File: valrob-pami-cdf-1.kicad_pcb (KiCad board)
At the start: 4 copper layers, 58 x 50 mm, 139 parts, among them J1 Conn_01x04, J2 USB_C_Receptacle_USB2.0_14P, J3 Conn_01x02, J4 Conn_01x04_Pin, J5 Conn_01x06, M1 Motor_Servo, M2 Stepper_Motor_bipolar, M3 Stepper_Motor_bipolar, Q1 Q_NMOS, Q2 Q_NMOS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

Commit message: schem/pcb: reorganize programmable gpios
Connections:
- U4 pad 10: /SDA -> /~{FAULT_1}
- U4 pad 11: /SCL -> unconnected-(U4-GPIO6/ADC1_CH5-Pad11)
- U4 pad 12: /DIR_1 -> /EMS
- U4 pad 13: /STEP_1 -> /VPWM_1
- U4 pad 14: /EN_1 -> /VPWM_2
- U4 pad 15: /~{SLEEP_1} -> /Vsense
- U4 pad 16: /~{FAULT_1} -> /DIR_2
- U4 pad 17: /DIR_2 -> /STEP_2
- U4 pad 18: /STEP_2 -> /EN_2
- U4 pad 19: /EN_2 -> /~{SLEEP_2}
- U4 pad 23: /~{SLEEP_2} -> /~{FAULT_2}
- U4 pad 24: /~{FAULT_2} -> /BUZZER
- U4 pad 27: /BUZZER -> /RGB1
- U4 pad 36: /RGB1 -> /SCL
- U4 pad 37: /SERVO1 -> /SDA
- U4 pad 43: unconnected-(U4-GPIO38-Pad43) -> /SERVO1
- U4 pad 6: /EMS -> /DIR_1
- U4 pad 7: /Vsense -> /STEP_1
- U4 pad 8: /VPWM_1 -> /EN_1
- U4 pad 9: /VPWM_2 -> /~{SLEEP_1}
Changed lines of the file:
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@@
 	(net 109 "unconnected-(U4-MTDO{slash}JTAG{slash}GPIO40-Pad45)")
 	(net 110 "unconnected-(U4-GPIO45-Pad51)")
-	(net 111 "unconnected-(U4-GPIO38-Pad43)")
-	(net 112 "unconnected-(U4-SPIQ{slash}GPIO31-Pad34)")
-	(net 113 "/~{SLEEP_2}")
-	(net 114 "unconnected-(U4-GPIO16{slash}ADC2_CH5{slash}XTAL_32K_N-Pad22)")
-	(net 115 "unconnected-(U4-MTDI{slash}JTAG{slash}GPIO41-Pad47)")
-	(net 116 "unconnected-(U6-M1-Pad17)")
-	(net 117 "unconnected-(U6-TOFF-Pad14)")
-	(net 118 "unconnected-(U7-TOFF-Pad14)")
-	(net 119 "unconnected-(U7-M1-Pad17)")
-	(net 120 "unconnected-(D1-DOUT-Pad2)")
-	(net 121 "Net-(J5-Pin_5)")
-	(net 122 "Net-(J5-Pin_4)")
-	(net 123 "Net-(J5-Pin_2)")
-	(net 124 "Net-(J5-Pin_3)")
+	(net 111 "unconnected-(U4-SPIQ{slash}GPIO31-Pad34)")
+	(net 112 "/~{SLEEP_2}")
+	(net 113 "unconnected-(U4-GPIO16{slash}ADC2_CH5{slash}XTAL_32K_N-Pad22)")
+	(net 114 "unconnected-(U4-MTDI{slash}JTAG{slash}GPIO41-Pad47)")
+	(net 115 "unconnected-(U6-M1-Pad17)")
+	(net 116 "unconnected-(U6-TOFF-Pad14)")
+	(net 117 "unconnected-(U7-TOFF-Pad14)")
+	(net 118 "unconnected-(U7-M1-Pad17)")
+	(net 119 "unconnected-(D1-DOUT-Pad2)")
+	(net 120 "Net-(J5-Pin_5)")
+	(net 121 "Net-(J5-Pin_4)")
+	(net 122 "Net-(J5-Pin_2)")
+	(net 123 "Net-(J5-Pin_3)")
+	(net 124 "unconnected-(U4-GPIO6{slash}ADC1_CH5-Pad11)")
 	(footprint "GLCS:Texas_RGE0024B_VQFN-24-1EP_4x4mm_P0.5mm_EP2.5x2.5mm_ThermalVias"
 		(layer "F.Cu")
@@
 			(layers "F.Cu" "F.Mask" "F.Paste")
 			(roundrect_rratio 0.25)
-			(net 117 "unconnected-(U6-TOFF-Pad14)")
+			(net 116 "unconnected-(U6-TOFF-Pad14)")
 			(pinfunction "TOFF")
 			(pintype "input+no_connect")
@@
 			(layers "F.Cu" "F.Mask" "F.Paste")
 			(roundrect_rratio 0.25)
-			(net 116 "unconnected-(U6-M1-Pad17)")
+			(net 115 "unconnected-(U6-M1-Pad17)")
 			(pinfunction "M1")
 			(pintype "input+no_connect")
@@
 			(layers "F.Cu" "F.Mask" "F.Paste")
 			(roundrect_rratio 0.1)
-			(net 120 "unconnected-(D1-DOUT-Pad2)")
+			(net 119 "unconnected-(D1-DOUT-Pad2)")
 			(pinfunction "DOUT")
 			(pintype "output+no_connect")
@@
 			(layers "F.Cu" "F.Mask" "F.Paste")
 			(roundrect_rratio 0.25)
-			(net 118 "unconnected-(U7-TOFF-Pad14)")
+			(net 117 "unconnected-(U7-TOFF-Pad14)")
 			(pinfunction "TOFF")
 			(pintype "input+no_connect")
@@
 			(layers "F.Cu" "F.Mask" "F.Paste")
 			(roundrect_rratio 0.25)
-			(net 119 "unconnected-(U7-M1-Pad17)")
+			(net 118 "unconnected-(U7-M1-Pad17)")
 			(pinfunction "M1")
 			(pintype "input+no_connect")
@@
 			(layers "F.Cu" "F.Mask" "F.Paste")
 			(roundrect_rratio 0.25)
-			(net 113 "/~{SLEEP_2}")
+			(net 112 "/~{SLEEP_2}")
 			(pinfunction "~{SLEEP}")
 			(pintype "input")
@@
 			(layers "F.Cu" "F.Mask" "F.Paste")
 			(roundrect_rratio 0.25)
-			(net 87 "/EMS")
+			(net 93 "/DIR_1")
 			(pinfunction "GPIO1/ADC1_CH0")
 			(pintype "bidirectional")
@@
 			(layers "F.Cu" "F.Mask" "F.Paste")
 			(roundrect_rratio 0.25)
-			(net 23 "/Vsense")
+			(net 88 "/STEP_1")
 			(pinfunction "GPIO2/ADC1_CH1")
 			(pintype "bidirectional")
@@
 			(layers "F.Cu" "F.Mask" "F.Paste")
 			(roundrect_rratio 0.25)
-			(net 84 "/VPWM_1")
+			(net 100 "/EN_1")
 			(pinfunction "GPIO3/ADC1_CH2")
 			(pintype "bidirectional")
@@
 			(layers "F.Cu" "F.Mask" "F.Paste")
 			(roundrect_rratio 0.25)
-			(net 86 "/VPWM_2")
+			(net 99 "/~{SLEEP_1}")
 			(pinfunction "GPIO4/ADC1_CH3")
 			(pintype "bidirectional")
@@
 			(layers "F.Cu" "F.Mask" "F.Paste")
 			(roundrect_rratio 0.25)
-			(net 81 "/SDA")
+			(net 83 "/~{FAULT_1}")
 			(pinfunction "GPIO5/ADC1_CH4")
 			(pintype "bidirectional")
@@
 			(layers "F.Cu" "F.Mask" "F.Paste")
 			(roundrect_rratio 0.25)
-			(net 82 "/SCL")
+			(net 124 "unconnected-(U4-GPIO6{slash}ADC1_CH5-Pad11)")
 			(pinfunction "GPIO6/ADC1_CH5")
 			(pintype "bidirectional")
@@
 			(layers "F.Cu" "F.Mask" "F.Paste")
 			(roundrect_rratio 0.25)
-			(net 93 "/DIR_1")
+			(net 87 "/EMS")
 			(pinfunction "GPIO7/ADC1_CH6")
 			(pintype "bidirectional")
@@
 			(layers "F.Cu" "F.Mask" "F.Paste")
 			(roundrect_rratio 0.25)
-			(net 88 "/STEP_1")
+			(net 84 "/VPWM_1")
 			(pinfunction "GPIO8/ADC1_CH7")
 			(pintype "bidirectional")
@@
 			(layers "F.Cu" "F.Mask" "F.Paste")
 			(roundrect_rratio 0.25)
-			(net 100 "/EN_1")
+			(net 86 "/VPWM_2")
 			(pinfunction "GPIO9/ADC1_CH8")
 			(pintype "bidirectional")
@@
 			(layers "F.Cu" "F.Mask" "F.Paste")
 			(roundrect_rratio 0.25)
-			(net 99 "/~{SLEEP_1}")
+			(net 23 "/Vsense")
 			(pinfunction "GPIO10/ADC1_CH9")
 			(pintype "bidirectional")
@@
 			(layers "F.Cu" "F.Mask" "F.Paste")
 			(roundrect_rratio 0.25)
-			(net 83 "/~{FAULT_1}")
+			(net 104 "/DIR_2")
 			(pinfunction "GPIO11/ADC2_CH0")
 			(pintype "bidirectional")
@@
 			(layers "F.Cu" "F.Mask" "F.Paste")
 			(roundrect_rratio 0.25)
-			(net 104 "/DIR_2")
+			(net 97 "/STEP_2")
 			(pinfunction "GPIO12/ADC2_CH1")
 			(pintype "bidirectional")
@@
 			(layers "F.Cu" "F.Mask" "F.Paste")
 			(roundrect_rratio 0.25)
-			(net 97 "/STEP_2")
+			(net 106 "/EN_2")
 			(pinfunction "GPIO13/ADC2_CH2")
 			(pintype "bidirectional")
@@
 			(layers "F.Cu" "F.Mask" "F.Paste")
 			(roundrect_rratio 0.25)
-			(net 106 "/EN_2")
+			(net 112 "/~{SLEEP_2}")
 			(pinfunction "GPIO14/ADC2_CH3")
 			(pintype "bidirectional")
@@
 			(layers "F.Cu" "F.Mask" "F.Paste")
 			(roundrect_rratio 0.25)
-			(net 114 "unconnected-(U4-GPIO16{slash}ADC2_CH5{slash}XTAL_32K_N-Pad22)")
+			(net 113 "unconnected-(U4-GPIO16{slash}ADC2_CH5{slash}XTAL_32K_N-Pad22)")
 			(pinfunction "GPIO16/ADC2_CH5/XTAL_32K_N")
 			(pintype "bidirectional+no_connect")
@@
 			(layers "F.Cu" "F.Mask" "F.Paste")
 			(roundrect_rratio 0.25)
-			(net 113 "/~{SLEEP_2}")
+			(net 85 "/~{FAULT_2}")
 			(pinfunction "GPIO17/ADC2_CH6")
 			(pintype "bidirectional")
@@
 			(layers "F.Cu" "F.Mask" "F.Paste")
 			(roundrect_rratio 0.25)
-			(net 85 "/~{FAULT_2}")
+			(net 75 "/BUZZER")
 			(pinfunction "GPIO18/ADC2_CH7")
 			(pintype "bidirectional")
@@
 			(layers "F.Cu" "F.Mask" "F.Paste")
 			(roundrect_rratio 0.25)
-			(net 75 "/BUZZER")
+			(net 37 "/RGB1")
 			(pinfunction "GPIO21")
 			(pintype "bidirectional")
@@
 			(layers "F.Cu" "F.Mask" "F.Paste")
 			(roundrect_rratio 0.25)
-			(net 112 "unconnected-(U4-SPIQ{slash}GPIO31-Pad34)")
+			(net 111 "unconnected-(U4-SPIQ{slash}GPIO31-Pad34)")
 			(pinfunction "SPIQ/GPIO31")
 			(pintype "bidirectional+no_connect")
@@
 			(layers "F.Cu" "F.Mask" "F.Paste")
 			(roundrect_rratio 0.25)
-			(net 37 "/RGB1")
+			(net 82 "/SCL")
 			(pinfunction "SPICLK_N/GPIO48")
 			(pintype "bidirectional")
@@
 			(layers "F.Cu" "F.Mask" "F.Paste")
 			(roundrect_rratio 0.25)
-			(net 54 "/SERVO1")
+			(net 81 "/SDA")
 			(pinfunction "SPICLK_P/GPIO47")
 			(pintype "bidirectional")
@@
 			(layers "F.Cu" "F.Mask" "F.Paste")
 			(roundrect_rratio 0.25)
-			(net 123 "Net-(J5-Pin_2)")
+			(net 122 "Net-(J5-Pin_2)")
 			(pinfunction "GPIO34")
 			(pintype "bidirectional")
@@
 			(layers "F.Cu" "F.Mask" "F.Paste")
 			(roundrect_rratio 0.25)
-			(net 124 "Net-(J5-Pin_3)")
+			(net 123 "Net-(J5-Pin_3)")
 			(pinfunction "GPIO35")
 			(pintype "bidirectional")
@@
 			(layers "F.Cu" "F.Mask" "F.Paste")
 			(roundrect_rratio 0.25)
-			(net 122 "Net-(J5-Pin_4)")
+			(net 121 "Net-(J5-Pin_4)")
 			(pinfunction "GPIO36")
 			(pintype "bidirectional")
@@
 			(layers "F.Cu" "F.Mask" "F.Paste")
 			(roundrect_rratio 0.25)
-			(net 121 "Net-(J5-Pin_5)")
+			(net 120 "Net-(J5-Pin_5)")
 			(pinfunction "GPIO37")
 			(pintype "bidirectional")
@@
 			(layers "F.Cu" "F.Mask" "F.Paste")
 			(roundrect_rratio 0.25)
-			(net 111 "unconnected-(U4-GPIO38-Pad43)")
+			(net 54 "/SERVO1")
 			(pinfunction "GPIO38")
-			(pintype "bidirectional+no_connect")
+			(pintype "bidirectional")
 		)
 		(pad "44" smd roundrect
@@
 			(layers "F.Cu" "F.Mask" "F.Paste")
 			(roundrect_rratio 0.25)
-			(net 115 "unconnected-(U4-MTDI{slash}JTAG{slash}GPIO41-Pad47)")
+			(net 114 "unconnected-(U4-MTDI{slash}JTAG{slash}GPIO41-Pad47)")
 			(pinfunction "MTDI/JTAG/GPIO41")
 			(pintype "bidirectional+no_connect")
@@
 			(layers "*.Cu" "*.Mask")
 			(remove_unused_layers no)
-			(net 123 "Net-(J5-Pin_2)")
+			(net 122 "Net-(J5-Pin_2)")
 			(pinfunction "Pin_2")
 			(pintype "passive")
@@
 			(layers "*.Cu" "*.Mask")
 			(remove_unused_layers no)
-			(net 124 "Net-(J5-Pin_3)")
+			(net 123 "Net-(J5-Pin_3)")
 			(pinfunction "Pin_3")
 			(pintype "passive")
@@
 			(layers "*.Cu" "*.Mask")
 			(remove_unused_layers no)
-			(net 122 "Net-(J5-Pin_4)")
+			(net 121 "Net-(J5-Pin_4)")
 			(pinfunction "Pin_4")
 			(pintype "passive")
@@
 			(layers "*.Cu" "*.Mask")
 			(remove_unused_layers no)
-			(net 121 "Net-(J5-Pin_5)")
+			(net 120 "Net-(J5-Pin_5)")
 			(pinfunction "Pin_5")
 			(pintype "passive")

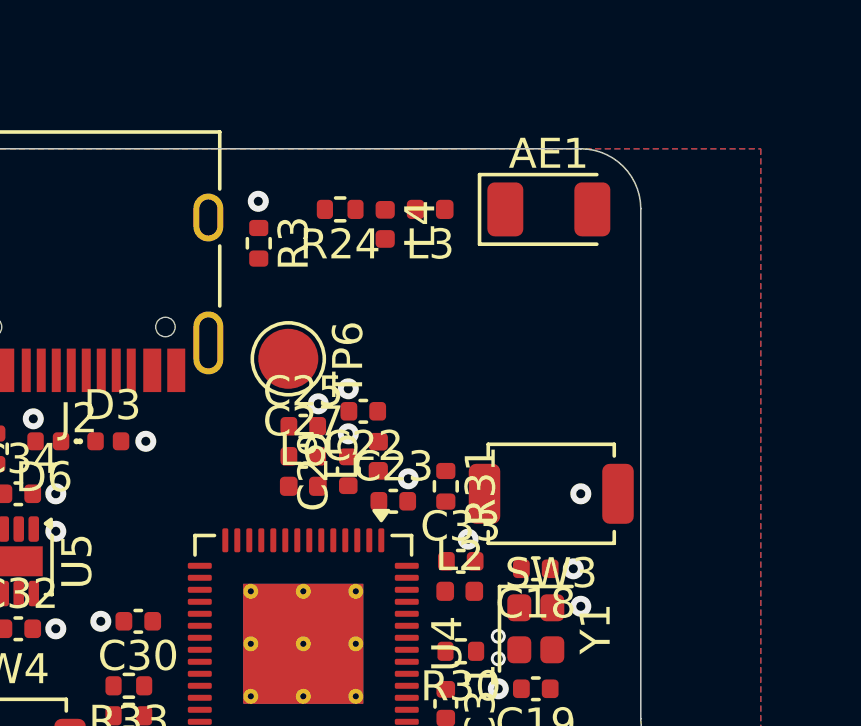
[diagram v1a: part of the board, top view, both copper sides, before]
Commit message: pcb: add rf routing
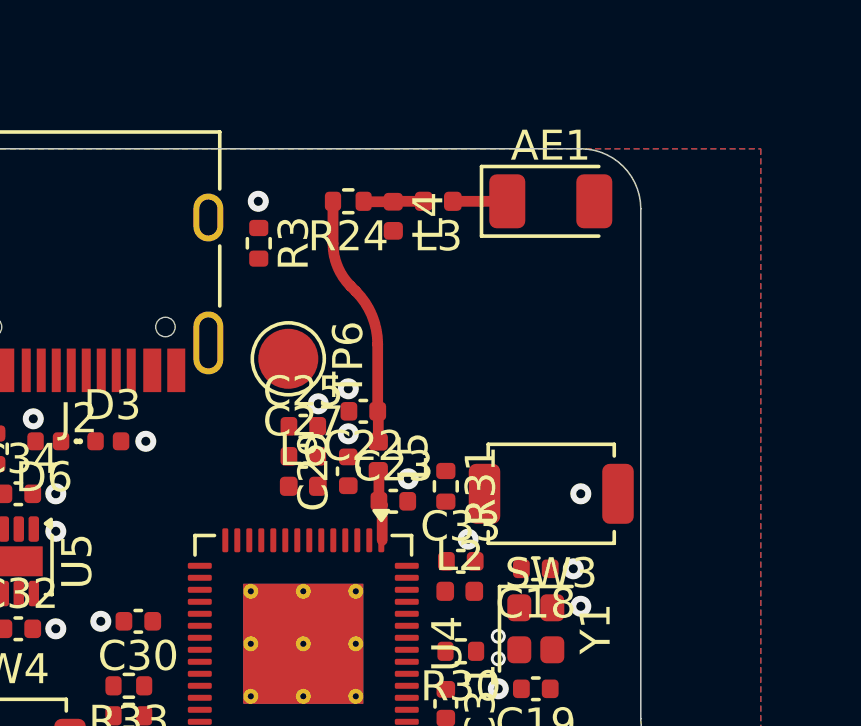
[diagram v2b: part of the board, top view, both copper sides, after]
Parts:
- moved L3 0.38 mm to (173.2, 74.8)
- moved L4 0.38 mm to (171.8, 75.2)
- moved R24 0.38 mm to (170.2, 74.8)
- moved AE1 0.28 mm to (177.0, 74.8)
- turned L5 to -90 degrees
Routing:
- net /RF_TRANS: track 0.00 -> 8.42 mm
- net /RF_ESP: track 0.00 -> 2.37 mm
- net Net-(L3-Pad2): track 0.00 -> 2.02 mm
- net /RF_ANT: track 0.00 -> 1.81 mm
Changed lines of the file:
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@@
 	(footprint "Inductor_SMD:L_0402_1005Metric"
 		(layer "F.Cu")
-		(at 171.25 83.25 90)
+		(at 171.25 83.25 -90)
 		(descr "Inductor SMD 0402 (1005 Metric), square (rectangular) end terminal, IPC-7351 nominal, (Body size source: http://www.tortai-tech.com/upload/download/2011102023233369053.pdf), generated with kicad-footprint-generator")
 		(tags "inductor")
@@
 		)
 		(property "Manufacturer" "Murata"
-			(at 0 0 90)
+			(at 0 0 270)
 			(unlocked yes)
 			(layer "F.Fab")
@@
 		)
 		(property "Manufacturer Part Number" "LQG15HS2N7S02D"
-			(at 0 0 90)
+			(at 0 0 270)
 			(unlocked yes)
 			(layer "F.Fab")
@@
 		)
 		(property "Basic" "X"
-			(at 0 0 90)
+			(at 0 0 270)
 			(unlocked yes)
 			(layer "F.Fab")
@@
 		)
 		(property "JLCPCB Part #" "C77108"
-			(at 0 0 90)
+			(at 0 0 270)
 			(unlocked yes)
 			(layer "F.Fab")
@@
 		)
 		(pad "1" smd roundrect
-			(at -0.485 0 90)
+			(at -0.485 0 270)
 			(size 0.59 0.64)
 			(layers "F.Cu" "F.Mask" "F.Paste")
@@
 		)
 		(pad "2" smd roundrect
-			(at 0.485 0 90)
+			(at 0.485 0 270)
 			(size 0.59 0.64)
 			(layers "F.Cu" "F.Mask" "F.Paste")
@@
 	(footprint "Inductor_SMD:L_0402_1005Metric"
 		(layer "F.Cu")
-		(at 172.98 75.02 180)
+		(at 173.25 74.75 180)
 		(descr "Inductor SMD 0402 (1005 Metric), square (rectangular) end terminal, IPC-7351 nominal, (Body size source: http://www.tortai-tech.com/upload/download/2011102023233369053.pdf), generated with kicad-footprint-generator")
 		(tags "inductor")
@@
 	(footprint "RF_Antenna:Johanson_2450AT18x100"
 		(layer "F.Cu")
-		(at 176.935 75.02)
+		(at 177 74.75)
 		(descr "Johanson 2450AT43F0100 SMD antenna 2400-2500Mhz, -0.5dBi, https://www.johansontechnology.com/datasheets/2450AT18A100/2450AT18A100.pdf")
 		(tags "antenna")
@@
 	(footprint "Inductor_SMD:L_0402_1005Metric"
 		(layer "F.Cu")
-		(at 171.48 75.52 -90)
+		(at 171.75 75.25 -90)
 		(descr "Inductor SMD 0402 (1005 Metric), square (rectangular) end terminal, IPC-7351 nominal, (Body size source: http://www.tortai-tech.com/upload/download/2011102023233369053.pdf), generated with kicad-footprint-generator")
 		(tags "inductor")
@@
 	(footprint "Resistor_SMD:R_0402_1005Metric"
 		(layer "F.Cu")
-		(at 169.98 75.02 180)
+		(at 170.25 74.75 180)
 		(descr "Resistor SMD 0402 (1005 Metric), square (rectangular) end terminal, IPC-7351 nominal, (Body size source: IPC-SM-782 page 72, https://www.pcb-3d.com/wordpress/wp-content/uploads/ipc-sm-782a_amendment_1_and_2.pdf), generated with kicad-footprint-generator")
 		(tags "resistor")
@@
 		(layer "Edge.Cuts")
 	)
+	(segment
+		(start 175.55 74.75)
+		(end 173.735 74.75)
+		(width 0.359)
+		(layer "F.Cu")
+		(net 1)
+	)
 	(via
 		(at 161 105.75)
@@
 		(net 4)
 	)
+	(segment
+		(start 169.74 74.75)
+		(end 169.74 76.161573)
+		(width 0.359)
+		(layer "F.Cu")
+		(net 20)
+	)
+	(segment
+		(start 171.25 82.765)
+		(end 171.25 81.77)
+		(width 0.359)
+		(layer "F.Cu")
+		(net 20)
+	)
+	(segment
+		(start 171.25 81.77)
+		(end 171.23 81.75)
+		(width 0.359)
+		(layer "F.Cu")
+		(net 20)
+	)
+	(segment
+		(start 171.23 79.515534)
+		(end 171.23 81.75)
+		(width 0.359)
+		(layer "F.Cu")
+		(net 20)
+	)
+	(segment
+		(start 170.325787 77.575787)
+		(end 170.497767 77.747767)
+		(width 0.359)
+		(layer "F.Cu")
+		(net 20)
+	)
+	(arc
+		(start 169.74 76.161573)
+		(mid 169.892241 76.92694)
+		(end 170.325787 77.575787)
+		(width 0.359)
+		(layer "F.Cu")
+		(net 20)
+	)
+	(arc
+		(start 171.23 79.515534)
+		(mid 171.039699 78.558825)
+		(end 170.497767 77.747767)
+		(width 0.359)
+		(layer "F.Cu")
+		(net 20)
+	)
+	(segment
+		(start 171.3805 84.8605)
+		(end 171.3805 86.05)
+		(width 0.359)
+		(layer "F.Cu")
+		(net 21)
+	)
+	(segment
+		(start 171.27 83.755)
+		(end 171.25 83.735)
+		(width 0.359)
+		(layer "F.Cu")
+		(net 21)
+	)
+	(segment
+		(start 171.27 84.75)
+		(end 171.27 83.755)
+		(width 0.359)
+		(layer "F.Cu")
+		(net 21)
+	)
+	(segment
+		(start 171.27 84.75)
+		(end 171.3805 84.8605)
+		(width 0.359)
+		(layer "F.Cu")
+		(net 21)
+	)
+	(segment
+		(start 171.765 74.75)
+		(end 171.75 74.765)
+		(width 0.359)
+		(layer "F.Cu")
+		(net 53)
+	)
+	(segment
+		(start 172.765 74.75)
+		(end 171.765 74.75)
+		(width 0.359)
+		(layer "F.Cu")
+		(net 53)
+	)
+	(segment
+		(start 170.775 74.765)
+		(end 170.76 74.75)
+		(width 0.359)
+		(layer "F.Cu")
+		(net 53)
+	)
+	(segment
+		(start 171.75 74.765)
+		(end 170.775 74.765)
+		(width 0.359)
+		(layer "F.Cu")
+		(net 53)
+	)
 	(zone

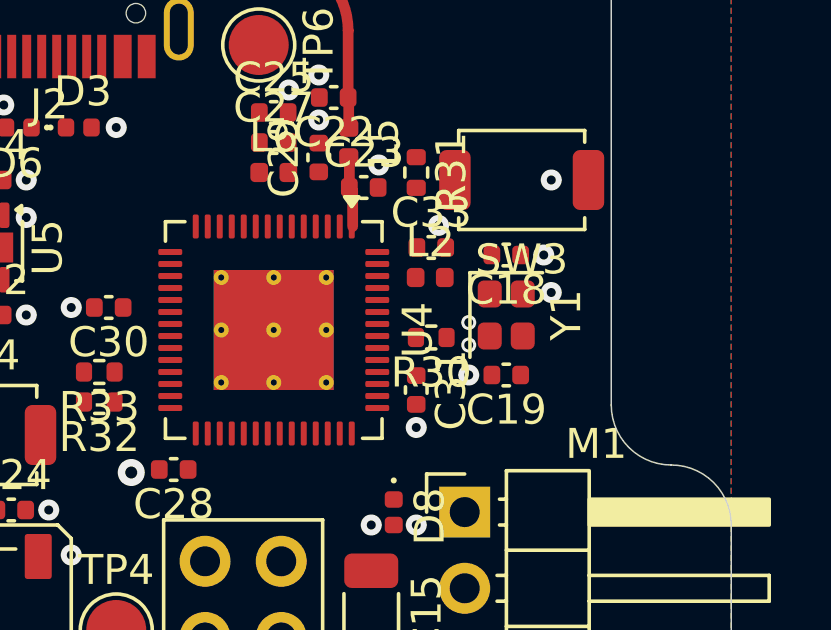
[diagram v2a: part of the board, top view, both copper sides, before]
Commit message: pcb: add crystal routing
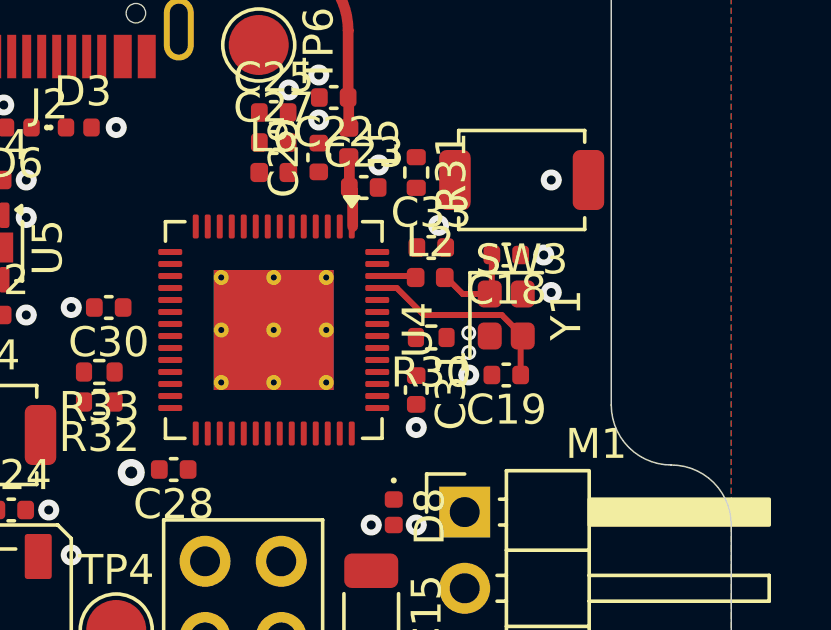
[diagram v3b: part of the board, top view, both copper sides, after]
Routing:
- net /XTAL_N: track 0.00 -> 6.84 mm
- net /XTAL_PL: track 0.00 -> 3.06 mm
- net /XTAL_P: track 0.00 -> 1.30 mm
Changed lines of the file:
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@@
 	)
 	(via
-		(at 175.25 89.25)
+		(at 175.25 89.599997)
 		(size 0.5)
 		(drill 0.3)
@@
 	)
 	(via
-		(at 175.25 90)
+		(at 175.25 90.25)
 		(size 0.5)
 		(drill 0.3)
@@
 		(free yes)
 		(net 4)
+	)
+	(segment
+		(start 174.5 87.75)
+		(end 175.05 88.3)
+		(width 0.2)
+		(layer "F.Cu")
+		(net 18)
+	)
+	(segment
+		(start 175.05 88.3)
+		(end 175.95 88.3)
+		(width 0.2)
+		(layer "F.Cu")
+		(net 18)
+	)
+	(segment
+		(start 176.02 88.23)
+		(end 175.95 88.3)
+		(width 0.2)
+		(layer "F.Cu")
+		(net 18)
+	)
+	(segment
+		(start 174.45 87.75)
+		(end 174.5 87.75)
+		(width 0.2)
+		(layer "F.Cu")
+		(net 18)
+	)
+	(segment
+		(start 176.02 87)
+		(end 176.02 88.23)
+		(width 0.2)
+		(layer "F.Cu")
+		(net 18)
+	)
+	(segment
+		(start 176.98 89.77)
+		(end 177.05 89.7)
+		(width 0.2)
+		(layer "F.Cu")
+		(net 19)
+	)
+	(segment
+		(start 176.98 91)
+		(end 176.98 89.77)
+		(width 0.2)
+		(layer "F.Cu")
+		(net 19)
+	)
+	(segment
+		(start 176.35 89)
+		(end 177.05 89.7)
+		(width 0.2)
+		(layer "F.Cu")
+		(net 19)
+	)
+	(segment
+		(start 173.75 89)
+		(end 176.35 89)
+		(width 0.2)
+		(layer "F.Cu")
+		(net 19)
+	)
+	(segment
+		(start 172.85 88.1)
+		(end 173.75 89)
+		(width 0.2)
+		(layer "F.Cu")
+		(net 19)
+	)
+	(segment
+		(start 172.2 88.1)
+		(end 172.85 88.1)
+		(width 0.2)
+		(layer "F.Cu")
+		(net 19)
 	)
 	(segment
@@
 	)
 	(segment
+		(start 173.43 87.7)
+		(end 173.48 87.75)
+		(width 0.2)
+		(layer "F.Cu")
+		(net 52)
+	)
+	(segment
+		(start 172.2 87.7)
+		(end 173.43 87.7)
+		(width 0.2)
+		(layer "F.Cu")
+		(net 52)
+	)
+	(segment
 		(start 171.765 74.75)
 		(end 171.75 74.765)
@@
 	)
 	(zone
+		(net 0)
+		(net_name "")
+		(layer "F.Cu")
+		(hatch edge 0.5)
+		(connect_pads
+			(clearance 0)
+		)
+		(min_thickness 0.15)
+		(filled_areas_thickness no)
+		(keepout
+			(tracks allowed)
+			(vias allowed)
+			(pads allowed)
+			(copperpour not_allowed)
+			(footprints allowed)
+		)
+		(placement
+			(enabled no)
+			(sheetname "/")
+		)
+		(fill
+			(thermal_gap 0.35)
+			(thermal_bridge_width 0.35)
+		)
+		(polygon
+			(pts
+				(xy 177.5 86.5) (xy 178.25 87.25) (xy 178.25 90.75) (xy 177.5 91.5) (xy 175 91.5) (xy 174.75 91.25)
+				(xy 174.75 87.25) (xy 175.5 86.5)
+			)
+		)
+	)
+	(zone
